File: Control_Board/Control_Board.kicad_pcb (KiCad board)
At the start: 2 copper layers, 46.3 x 41.3 mm, 60 parts, among them J1 Conn_01x06, J2 Conn_01x04, J3 Conn_01x03, J4 GPS_ANT, J5 Conn_01x02, J6 Conn_01x02, SW2 SW_SPST, U1 STM32F446RCTx, U3 SN65HVD256D, U6 AP2204K-ADJ, U7 AP2204K-ADJ, U8 SN65HVD256D, U9 NEO-XM, Y3 8M, Y4 32.768k

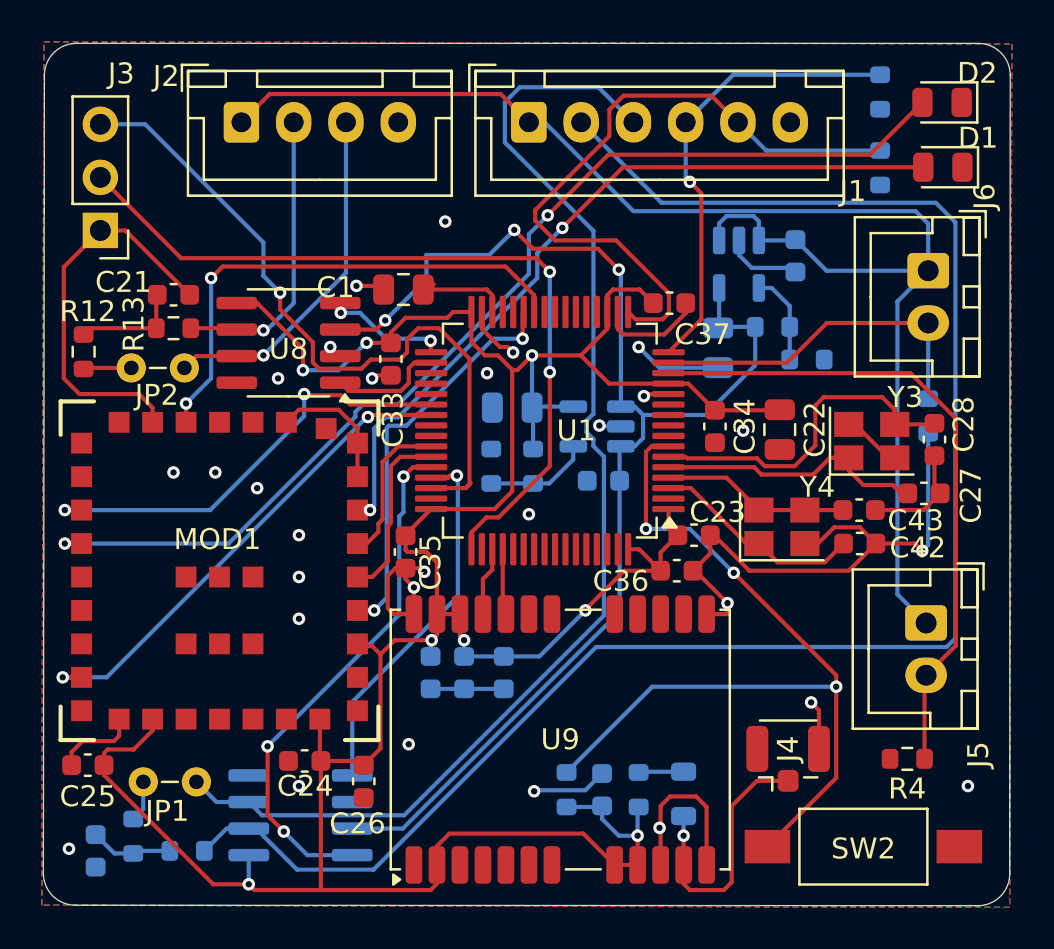
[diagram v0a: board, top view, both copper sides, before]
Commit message: fix(ctrl-board): add label on PCB
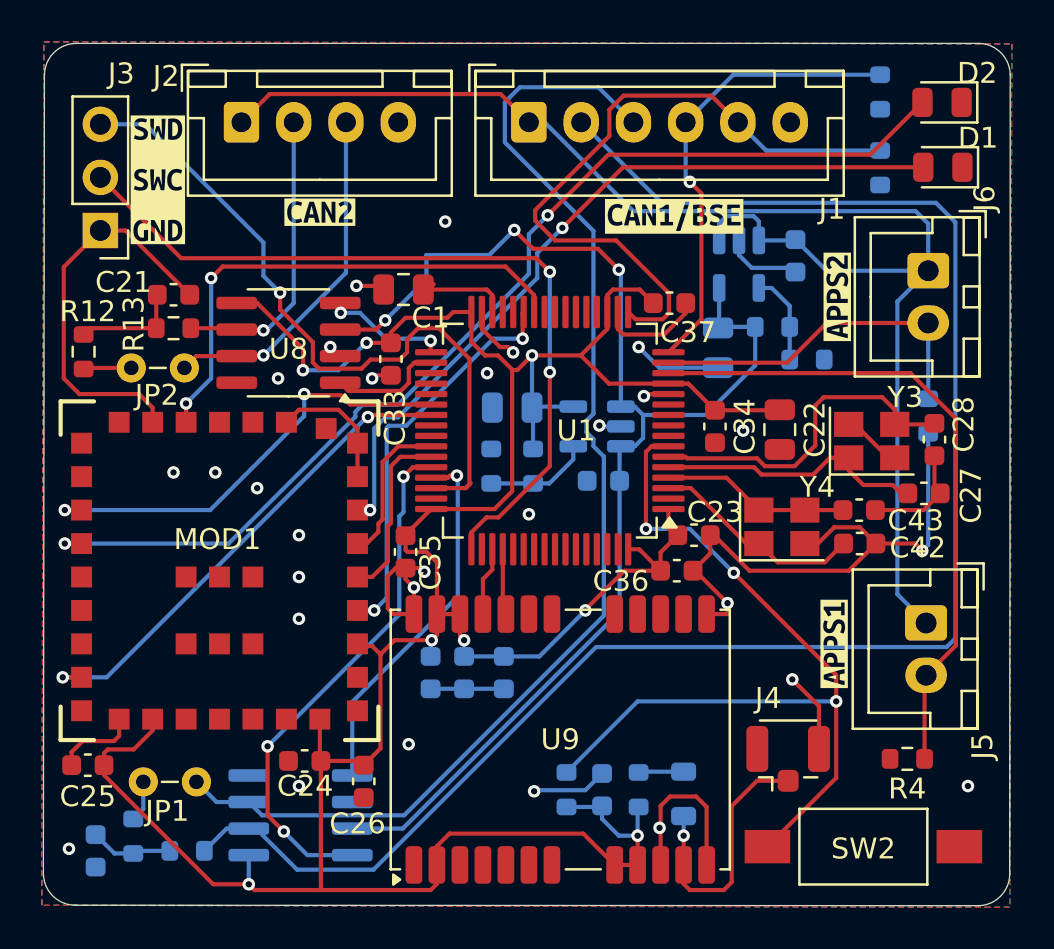
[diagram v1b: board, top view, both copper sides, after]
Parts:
- added kibuzzard-68852EE2: G***, kibuzzard-68852EE2, F.Cu at (58.2, 47.0)
- added kibuzzard-68852F9B: G***, kibuzzard-68852F9B, F.Cu at (90.6, 69.2)
- added kibuzzard-68852FF1: G***, kibuzzard-68852FF1, F.Cu at (90.8, 52.6)
- added kibuzzard-68853119: G***, kibuzzard-68853119, F.Cu at (66.0, 48.5)
- added kibuzzard-68853151: G***, kibuzzard-68853151, F.Cu at (83.0, 48.8)
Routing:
- net GND: track 111.2 -> 112.7 mm
